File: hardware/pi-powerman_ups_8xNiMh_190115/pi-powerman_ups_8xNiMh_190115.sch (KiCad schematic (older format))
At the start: 28 parts, among them J1 UPS_in, J2 UPS_out, J3 UPS_status, J4 UPS_bat, Q1 FDS6975, Q2 IRF7205, Q3 IRF7313PbF, Q4 TSM2318, U1 LTC4011

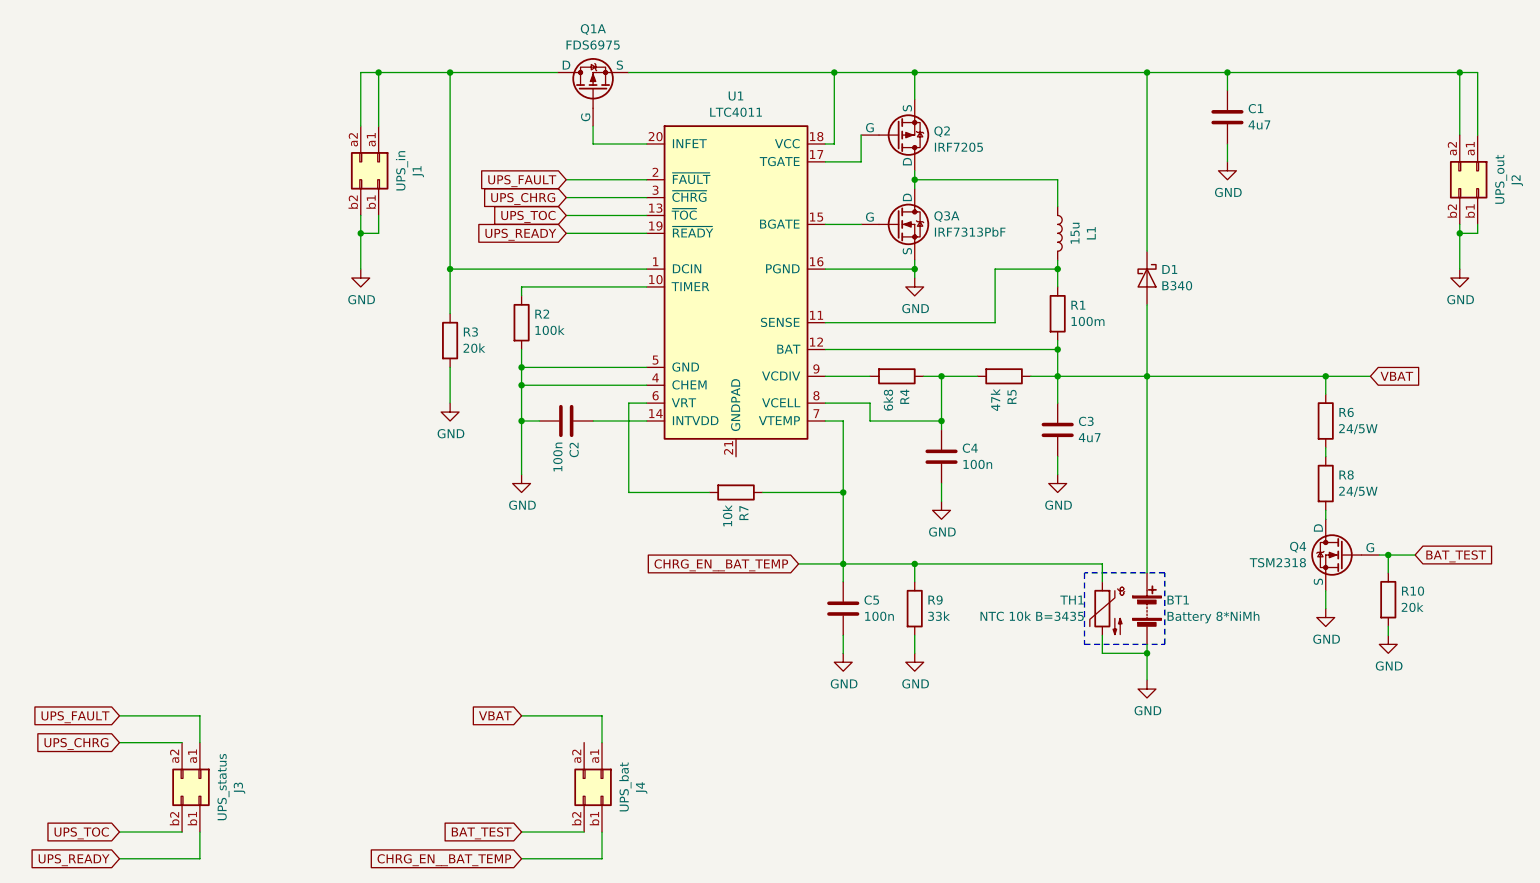
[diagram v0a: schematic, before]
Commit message: symbols update
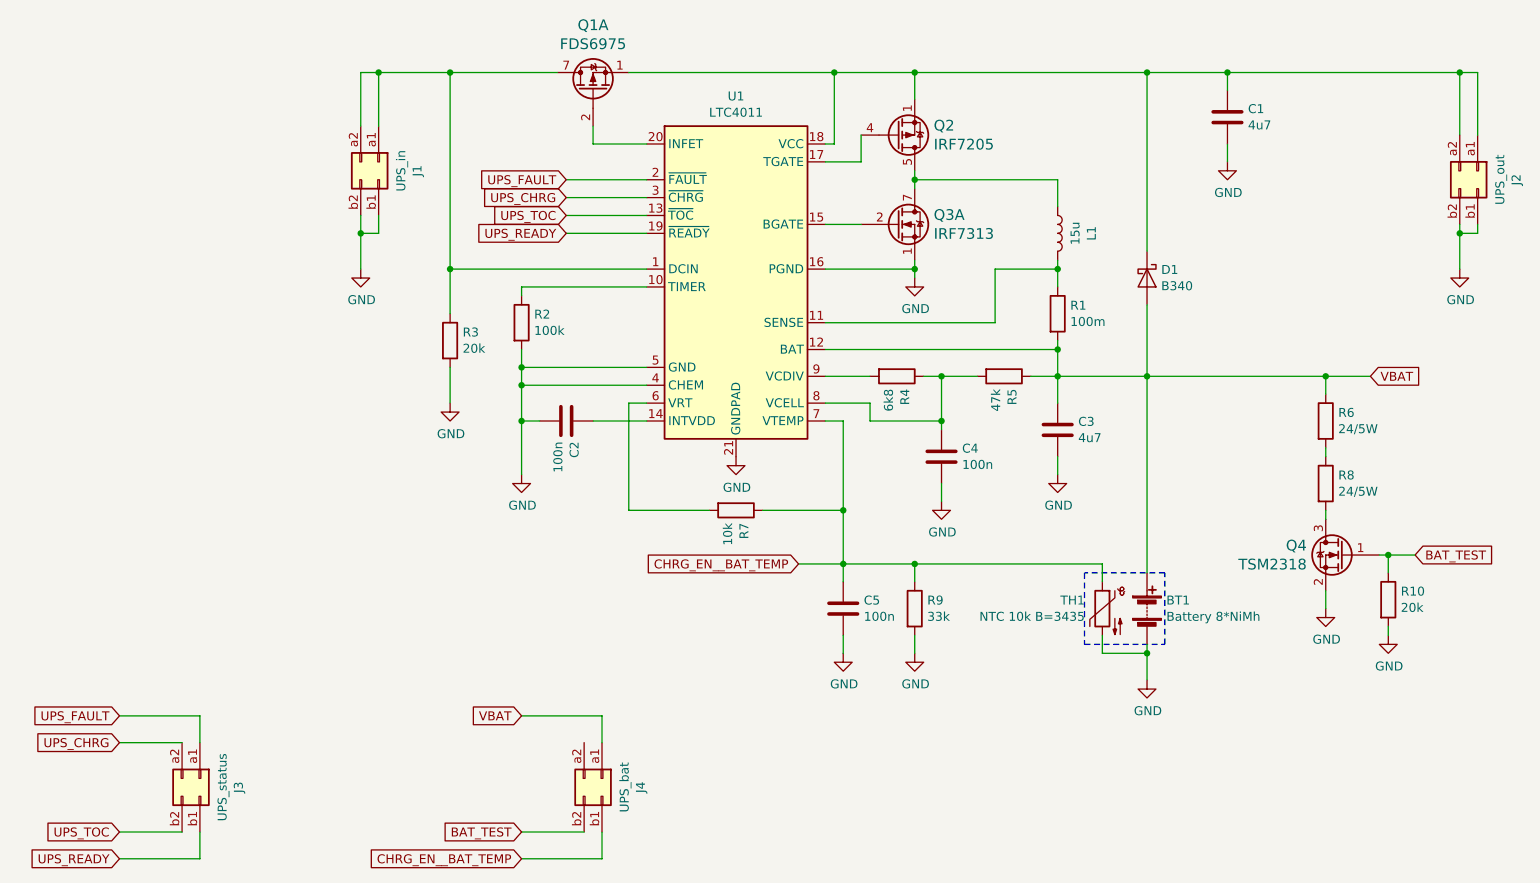
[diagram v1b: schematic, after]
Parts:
- removed Q1: FDS6975, symbol Transistor_FET_P-Channel:FDS6975
- removed Q2: IRF7205, symbol Transistor_FET_P-Channel:IRF7205
- removed Q3: IRF7313PbF, symbol Transistor_FET_N-Channel:IRF7313PbF
- removed Q4: TSM2318, symbol Transistor_FET_N-Channel:TSM2318
- removed U1: LTC4011, symbol ltc4011:LTC4011
- added Q1: FDS6975, Package_SO:SOIC-8_3.9x4.9mm_P1.27mm, symbol obbo_Transistors:FDS6975
- added Q2: IRF7205, Package_SO:SOIC-8_3.9x4.9mm_P1.27mm, symbol obbo_Transistors:IRF7205
- added Q3: IRF7313, Package_SO:SOIC-8_3.9x4.9mm_P1.27mm, symbol obbo_Transistors:IRF7313
- added Q4: TSM2318, obbo_footprints:SOT-23_HandSoldering, symbol obbo_Transistors:TSM2318
- added U1: LTC4011, obbo_footprints:TSSOP-20_4.4x6.5mm_P0.65mm_EP2.74x3.86mm, symbol obbo_IC:LTC4011
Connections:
- net BAT_TEST: now also Q4.1 (G)
- net CHRG_EN__BAT_TEMP: now also U1.7 (VTEMP)
- net GND: now also Q3.1 (S), Q4.2 (S), U1.16 (PGND), U1.21 (GNDPAD), U1.4 (CHEM), U1.5 (GND)
- net UPS_CHRG: now also U1.3 (~CHRG)
- net UPS_FAULT: now also U1.2 (~FAULT)
- net UPS_READY: now also U1.19 (~READY)
- net UPS_TOC: now also U1.13 (~TOC)
- net VBAT: now also U1.12 (BAT)
- net at L1.1, R1.1: now also U1.11 (SENSE)
- net at C4.1, R4.1, R5.2: now also U1.8 (VCELL)
- net at C1.1, D1.1 (K), J2.a1 (Pin_a1)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: now also Q1.1 (S), Q2.1 (S), Q2.2 (S), Q2.3 (S), U1.18 (VCC)
- net at L1.2: now also Q2.5 (D), Q2.6 (D), Q2.7 (D), Q2.8 (D), Q3.7 (D), Q3.8 (D)
- net at C2.1: now also U1.14 (INTVDD)
- net at J1.a1 (Pin_a1), J1.a2 (Pin_a2), R3.1: now also Q1.7 (D), Q1.8 (D), U1.1 (DCIN)
- net at R2.1: now also U1.10 (TIMER)
- net at R7.2: now also U1.6 (VRT)
- net at R4.2: now also U1.9 (VCDIV)
- net at R8.2: now also Q4.3 (D)
- new net: Q1.2 (G), U1.20 (INFET)
- new net: Q2.4 (G), U1.17 (TGATE)
- new net: Q3.2 (G), U1.15 (BGATE)
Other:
- moved on the sheet: R7
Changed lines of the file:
@@
 EESchema Schematic File Version 4
 LIBS:pi-powerman_ups_8xNiMh_190115-cache
-EELAYER 26 0
+EELAYER 30 0
 EELAYER END
 $Descr A4 11693 8268
@@
 	7550 5250 7550 5200
 $Comp
-L ltc4011:LTC4011 U1
-U 1 1 5CB2D07A
-P 5250 3150
-F 0 "U1" H 5250 4167 50  0000 C CNN
-F 1 "LTC4011" H 5250 4076 50  0000 C CNN
-F 2 "" H 5200 3100 50  0001 C CNN
-F 3 "" H 5200 3100 50  0001 C CNN
-	1    5250 3150
-	1    0    0    -1
-$EndComp
-$Comp
-L Transistor_FET_N-Channel:IRF7313PbF Q3
-U 1 1 5CB2EE06
-P 6200 2850
-F 0 "Q3" H 6356 2896 50  0000 L CNN
-F 1 "IRF7313PbF" H 6356 2805 50  0000 L CNN
-F 2 "" H 6200 2850 50  0001 C CNN
-F 3 "" H 6200 2850 50  0001 C CNN
-	1    6200 2850
-	1    0    0    -1
-$EndComp
-$Comp
-L Transistor_FET_N-Channel:TSM2318 Q4
-U 1 1 5CB2EF50
-P 8600 4700
-F 0 "Q4" H 8756 4746 50  0000 L CNN
-F 1 "TSM2318" H 8756 4655 50  0000 L CNN
-F 2 "" H 8600 4700 50  0001 C CNN
-F 3 "" H 8600 4700 50  0001 C CNN
-	1    8600 4700
-	-1   0    0    -1
-$EndComp
-$Comp
 L Device:R R8
 U 1 1 5CB2F0E4
@@
 Wire Wire Line
 	8550 4500 8550 4450
-$Comp
-L Transistor_FET_P-Channel:FDS6975 Q1
-U 1 1 5CB35274
-P 4450 2050
-F 0 "Q1" V 4743 2050 50  0000 C CNN
-F 1 "FDS6975" V 4652 2050 50  0000 C CNN
-F 2 "" H 4450 2050 50  0001 C CNN
-F 3 "" H 4450 2050 50  0001 C CNN
-	1    4450 2050
-	0    -1   -1   0
-$EndComp
 Wire Wire Line
 	4450 2300 4450 2400
 Wire Wire Line
 	4450 2400 4750 2400
-$Comp
-L Transistor_FET_P-Channel:IRF7205 Q2
-U 1 1 5CB35E3C
-P 6200 2350
-F 0 "Q2" H 6356 2329 50  0000 L CNN
-F 1 "IRF7205" H 6356 2420 50  0000 L CNN
-F 2 "" H 6200 2350 50  0001 C CNN
-F 3 "" H 6200 2350 50  0001 C CNN
-	1    6200 2350
-	1    0    0    1
-$EndComp
 Wire Wire Line
 	5750 2500 5950 2500
@@
 L Device:R R7
 U 1 1 5CB757CD
-P 5250 4350
-F 0 "R7" H 5320 4396 50  0000 L CNN
-F 1 "10k" H 5320 4305 50  0000 L CNN
-F 2 "" V 5180 4350 50  0001 C CNN
-F 3 "~" H 5250 4350 50  0001 C CNN
-	1    5250 4350
+P 5250 4450
+F 0 "R7" H 5320 4496 50  0000 L CNN
+F 1 "10k" H 5320 4405 50  0000 L CNN
+F 2 "" V 5180 4450 50  0001 C CNN
+F 3 "~" H 5250 4450 50  0001 C CNN
+	1    5250 4450
 	0    1    1    0
 $EndComp
@@
 	4750 3850 4650 3850
 Wire Wire Line
-	4650 3850 4650 4350
-Wire Wire Line
-	4650 4350 5100 4350
-Wire Wire Line
-	5400 4350 5850 4350
-Wire Wire Line
-	5850 4350 5850 3950
+	4650 3850 4650 4450
+Wire Wire Line
+	4650 4450 5100 4450
+Wire Wire Line
+	5400 4450 5850 4450
+Wire Wire Line
+	5850 4450 5850 3950
 Wire Wire Line
 	5850 3950 5750 3950
@@
 	5850 4750 5850 4850
 Wire Wire Line
-	5850 4750 5850 4350
+	5850 4750 5850 4450
 Connection ~ 5850 4750
-Connection ~ 5850 4350
+Connection ~ 5850 4450
 Wire Wire Line
 	6250 4850 6250 4750
@@
 Wire Notes Line
 	7650 4800 7200 4800
+$Comp
+L obbo_Transistors:TSM2318 Q4
+U 1 1 5DDB8B99
+P 8550 4700
+F 0 "Q4" H 8656 4753 60  0000 L CNN
+F 1 "TSM2318" H 8656 4647 60  0000 L CNN
+F 2 "obbo_footprints:SOT-23_HandSoldering" H 8650 4950 60  0001 L CIN
+F 3 "https://www.taiwansemi.com/products/datasheet/TSM2318_C15.pdf" H 8650 5000 60  0001 L CNN
+	1    8550 4700
+	-1   0    0    -1
+$EndComp
+$Comp
+L obbo_Transistors:FDS6975 Q1
+U 1 1 5DDD55D3
+P 4450 2000
+F 0 "Q1" V 4715 2000 60  0000 C CNN
+F 1 "FDS6975" V 4609 2000 60  0000 C CNN
+F 2 "Package_SO:SOIC-8_3.9x4.9mm_P1.27mm" H 4550 2250 60  0001 L CIN
+F 3 "https://www.onsemi.com/pub/Collateral/FDS6975-D.PDF" H 4650 2300 60  0001 L CNN
+	1    4450 2000
+	0    -1   -1   0
+$EndComp
+$Comp
+L obbo_Transistors:IRF7205 Q2
+U 1 1 5DDD6EB0
+P 6250 2350
+F 0 "Q2" H 6356 2297 60  0000 L CNN
+F 1 "IRF7205" H 6356 2403 60  0000 L CNN
+F 2 "Package_SO:SOIC-8_3.9x4.9mm_P1.27mm" H 6350 2600 60  0001 L CIN
+F 3 "http://www.irf.com/part/LEADED-30V-SINGLE-P-CHANNEL-HEXFET-POWER-MOSFET-IN-A-SO-8-PACKAGE/_/A~PB-IRF7205" H 6450 2650 60  0001 L CNN
+	1    6250 2350
+	1    0    0    1
+$EndComp
+$Comp
+L obbo_Transistors:IRF7313 Q3
+U 1 1 5DDDC7B8
+P 6250 2850
+F 0 "Q3" H 6356 2903 60  0000 L CNN
+F 1 "IRF7313" H 6356 2797 60  0000 L CNN
+F 2 "Package_SO:SOIC-8_3.9x4.9mm_P1.27mm" H 6350 3100 60  0001 L CIN
+F 3 "http://www.irf.com/part/LEADED-30V-DUAL-N-CHANNEL-HEXFET-POWER-MOSFET-IN-A-SO-8-PACKAGE/_/A~PB-IRF7313" H 6450 3150 60  0001 L CNN
+	1    6250 2850
+	1    0    0    -1
+$EndComp
+$Comp
+L obbo_IC:LTC4011 U1
+U 1 1 5DDE41B7
+P 5250 3150
+F 0 "U1" H 5250 4167 50  0000 C CNN
+F 1 "LTC4011" H 5250 4076 50  0000 C CNN
+F 2 "obbo_footprints:TSSOP-20_4.4x6.5mm_P0.65mm_EP2.74x3.86mm" H 5250 4150 50  0001 C CIN
+F 3 "https://www.analog.com/media/en/technical-documentation/data-sheets/4011fb.pdf" H 5200 3100 50  0001 C CNN
+	1    5250 3150
+	1    0    0    -1
+$EndComp
+$Comp
+L power:GND #PWR01
+U 1 1 5DDE89F6
+P 5250 4150
+F 0 "#PWR01" H 5250 3900 50  0001 C CNN
+F 1 "GND" H 5255 3977 50  0000 C CNN
+F 2 "" H 5250 4150 50  0001 C CNN
+F 3 "" H 5250 4150 50  0001 C CNN
+	1    5250 4150
+	1    0    0    -1
+$EndComp
 $EndSCHEMATC
